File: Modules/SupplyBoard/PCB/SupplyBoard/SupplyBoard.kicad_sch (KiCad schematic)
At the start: 4 parts, among them J1 CI_BATT, J2 USB_B_Mini, U1 STM32L031G6Ux

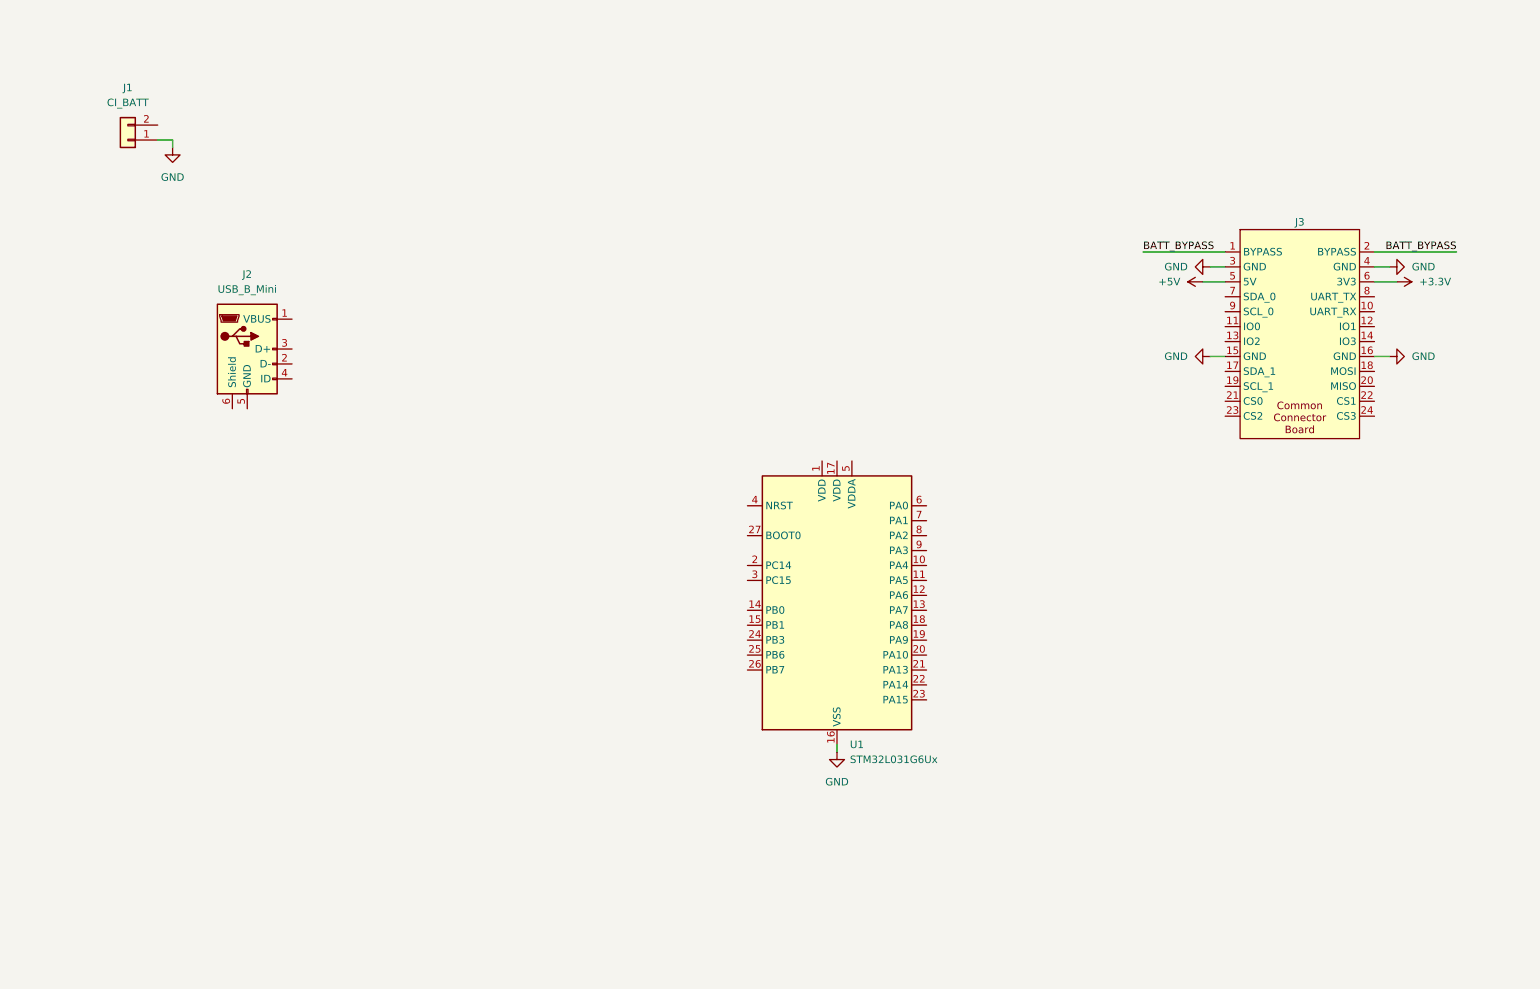
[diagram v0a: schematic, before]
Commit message: [Supply Board] Creados subesquemas
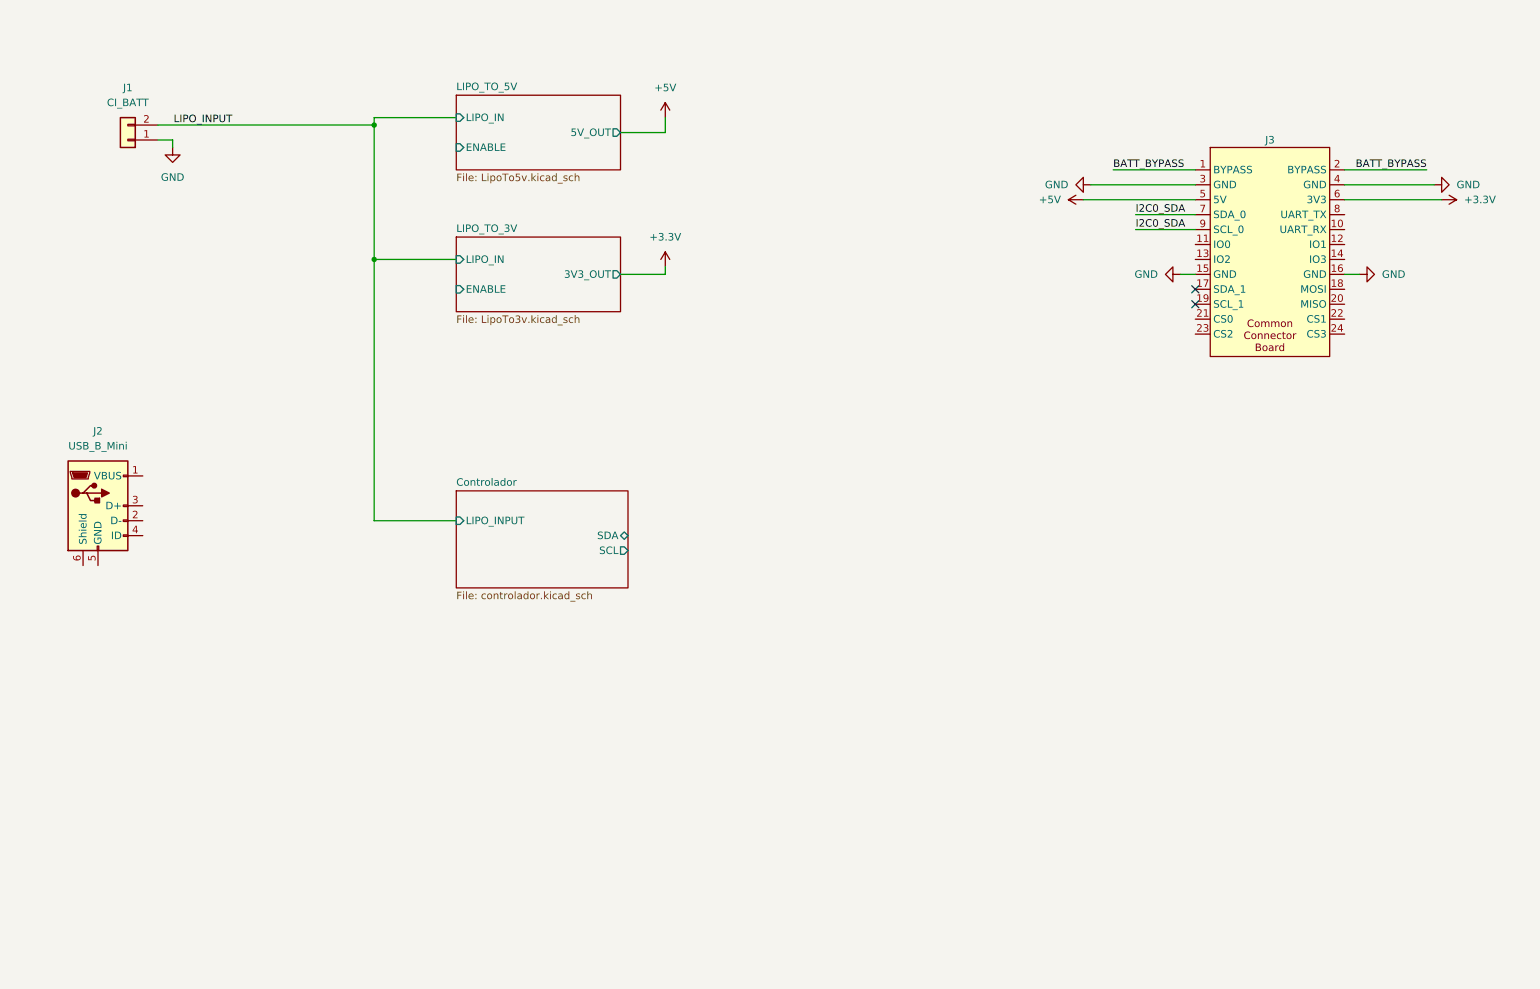
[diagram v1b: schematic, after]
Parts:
- removed U1: STM32L031G6Ux, Package_DFN_QFN:QFN-28_4x4mm_P0.5mm, symbol MCU_ST_STM32L0:STM32L031G6Ux
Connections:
- net LIPO_INPUT: now reaches J1.2 (Pin_2)
- net I2C0_SDA: now reaches J3.7 (SDA_0)
- net I2C0_SDA: now also J3.9 (SCL_0)
- no-connect marks 0 -> 2
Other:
- added sheet Controlador (controlador.kicad_sch)
- added sheet LIPO_TO_3V (LipoTo3v.kicad_sch)
- added sheet LIPO_TO_5V (LipoTo5v.kicad_sch)
- moved on the sheet: J2, J3

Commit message: Lipo to 3v3 circuit added
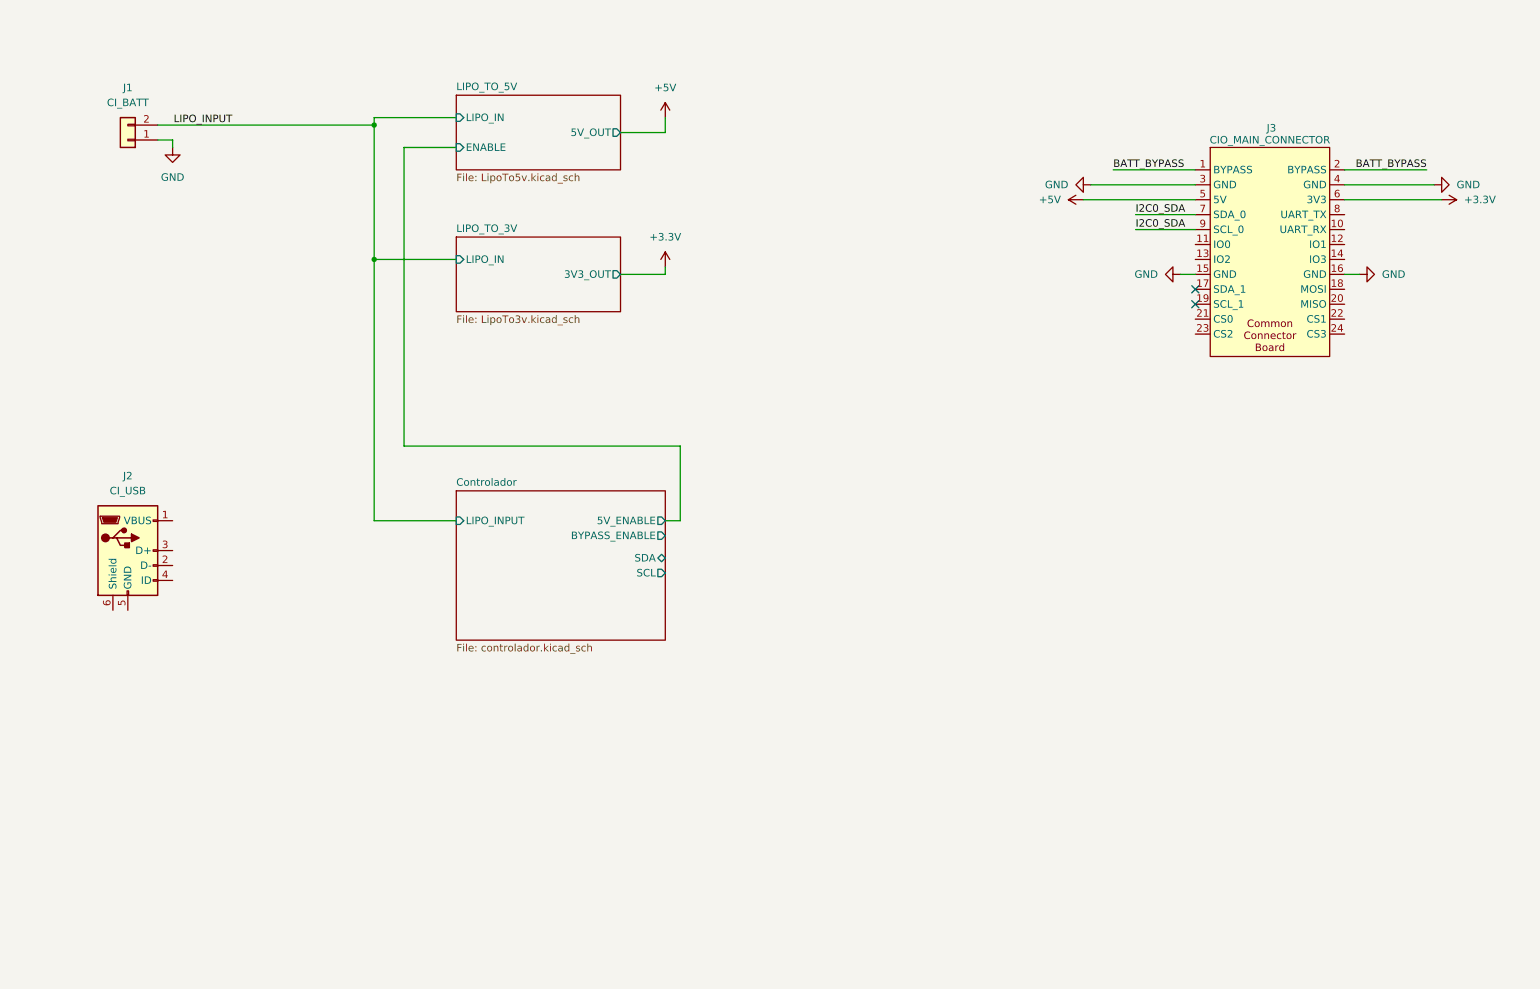
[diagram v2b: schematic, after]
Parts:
- J2: value USB_B_Mini -> CI_USB; footprint Connector_USB:USB_Micro-B_Wuerth_629105150521 -> (none)
- J3: value ~ -> CIO_MAIN_CONNECTOR
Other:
- sheet Controlador ports: added 5V_ENABLE, BYPASS_ENABLE; removed none
- sheet LIPO_TO_3V ports: added none; removed ENABLE
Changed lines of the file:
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@@
+	(wire
+		(pts
+			(xy 137.16 95.25) (xy 90.17 95.25)
+		)
+		(stroke
+			(width 0)
+			(type default)
+		)
+	)
+	(wire
+		(pts
+			(xy 134.62 107.95) (xy 137.16 107.95)
+		)
+		(stroke
+			(width 0)
+			(type default)
+		)
+	)
 	(wire
 		(pts
@@
 	(wire
 		(pts
+			(xy 90.17 44.45) (xy 99.06 44.45)
+		)
+		(stroke
+			(width 0)
+			(type default)
+		)
+	)
+	(wire
+		(pts
 			(xy 250.19 50.8) (xy 265.43 50.8)
 		)
@@
 	(wire
 		(pts
+			(xy 137.16 107.95) (xy 137.16 95.25)
+		)
+		(stroke
+			(width 0)
+			(type default)
+		)
+	)
+	(wire
+		(pts
 			(xy 214.63 55.88) (xy 224.79 55.88)
+		)
+		(stroke
+			(width 0)
+			(type default)
+		)
+	)
+	(wire
+		(pts
+			(xy 90.17 95.25) (xy 90.17 44.45)
 		)
 		(stroke
@@
 	(symbol
 		(lib_id "Connector:USB_B_Mini")
-		(at 38.1 105.41 0)
+		(at 43.18 113.03 0)
 		(unit 1)
 		(exclude_from_sim no)
@@
 		(fields_autoplaced yes)
 		(property "Reference" "J2"
-			(at 38.1 92.71 0)
-			(effects
-				(font
-					(size 1.27 1.27)
-				)
-			)
-		)
-		(property "Value" "USB_B_Mini"
-			(at 38.1 95.25 0)
-			(effects
-				(font
-					(size 1.27 1.27)
-				)
-			)
-		)
-		(property "Footprint" "Connector_USB:USB_Micro-B_Wuerth_629105150521"
-			(at 41.91 106.68 0)
-			(effects
-				(font
-					(size 1.27 1.27)
-				)
-				(hide yes)
-			)
-		)
-		(property "Datasheet" "https://www.lcsc.com/datasheet/lcsc_datasheet_2209301830_SHOU-HAN-MICRO5P-4J-ZB-X_C5184249.pdf"
-			(at 41.91 106.68 0)
+			(at 43.18 100.33 0)
+			(effects
+				(font
+					(size 1.27 1.27)
+				)
+			)
+		)
+		(property "Value" "CI_USB"
+			(at 43.18 102.87 0)
+			(effects
+				(font
+					(size 1.27 1.27)
+				)
+			)
+		)
+		(property "Footprint" ""
+			(at 46.99 114.3 0)
+			(effects
+				(font
+					(size 1.27 1.27)
+				)
+				(hide yes)
+			)
+		)
+		(property "Datasheet" "~"
+			(at 46.99 114.3 0)
 			(effects
 				(font
@@
 		)
 		(property "Description" "USB Mini Type B connector"
-			(at 38.1 105.41 0)
-			(effects
-				(font
-					(size 1.27 1.27)
-				)
-				(hide yes)
-			)
+			(at 43.18 113.03 0)
+			(effects
+				(font
+					(size 1.27 1.27)
+				)
+				(hide yes)
+			)
+		)
+		(pin "4"
 		)
 		(pin "5"
 		)
+		(pin "6"
+		)
 		(pin "2"
 		)
-		(pin "4"
+		(pin "1"
 		)
 		(pin "3"
-		)
-		(pin "6"
-		)
-		(pin "1"
 		)
 		(instances
@@
 		(dnp no)
 		(property "Reference" "J3"
-			(at 237.49 43.18 0)
-			(effects
-				(font
-					(size 1.27 1.27)
-				)
-			)
-		)
-		(property "Value" "~"
+			(at 237.744 41.148 0)
+			(effects
+				(font
+					(size 1.27 1.27)
+				)
+			)
+		)
+		(property "Value" "CIO_MAIN_CONNECTOR"
 			(at 237.49 43.18 0)
 			(effects
@@
 	(sheet
 		(at 99.06 102.87)
-		(size 29.21 16.51)
+		(size 35.56 25.4)
 		(fields_autoplaced yes)
 		(stroke
@@
 		)
 		(property "Sheetfile" "controlador.kicad_sch"
-			(at 99.06 119.9646 0)
+			(at 99.06 128.8546 0)
 			(effects
 				(font
@@
 		)
 		(pin "SCL" output
-			(at 128.27 113.03 0)
+			(at 134.62 116.84 0)
 			(effects
 				(font
@@
 		)
 		(pin "SDA" bidirectional
-			(at 128.27 110.49 0)
+			(at 134.62 114.3 0)
 			(effects
 				(font
@@
 				)
 				(justify left)
+			)
+		)
+		(pin "5V_ENABLE" output
+			(at 134.62 107.95 0)
+			(effects
+				(font
+					(size 1.27 1.27)
+				)
+				(justify right)
+			)
+		)
+		(pin "BYPASS_ENABLE" output
+			(at 134.62 110.49 0)
+			(effects
+				(font
+					(size 1.27 1.27)
+				)
+				(justify right)
 			)
 		)
@@
 			)
 		)
-		(pin "ENABLE" input
-			(at 99.06 68.58 180)
-			(effects
-				(font
-					(size 1.27 1.27)
-				)
-				(justify left)
-			)
-		)

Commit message: SupplyBoard - Added INA2180 current sensor
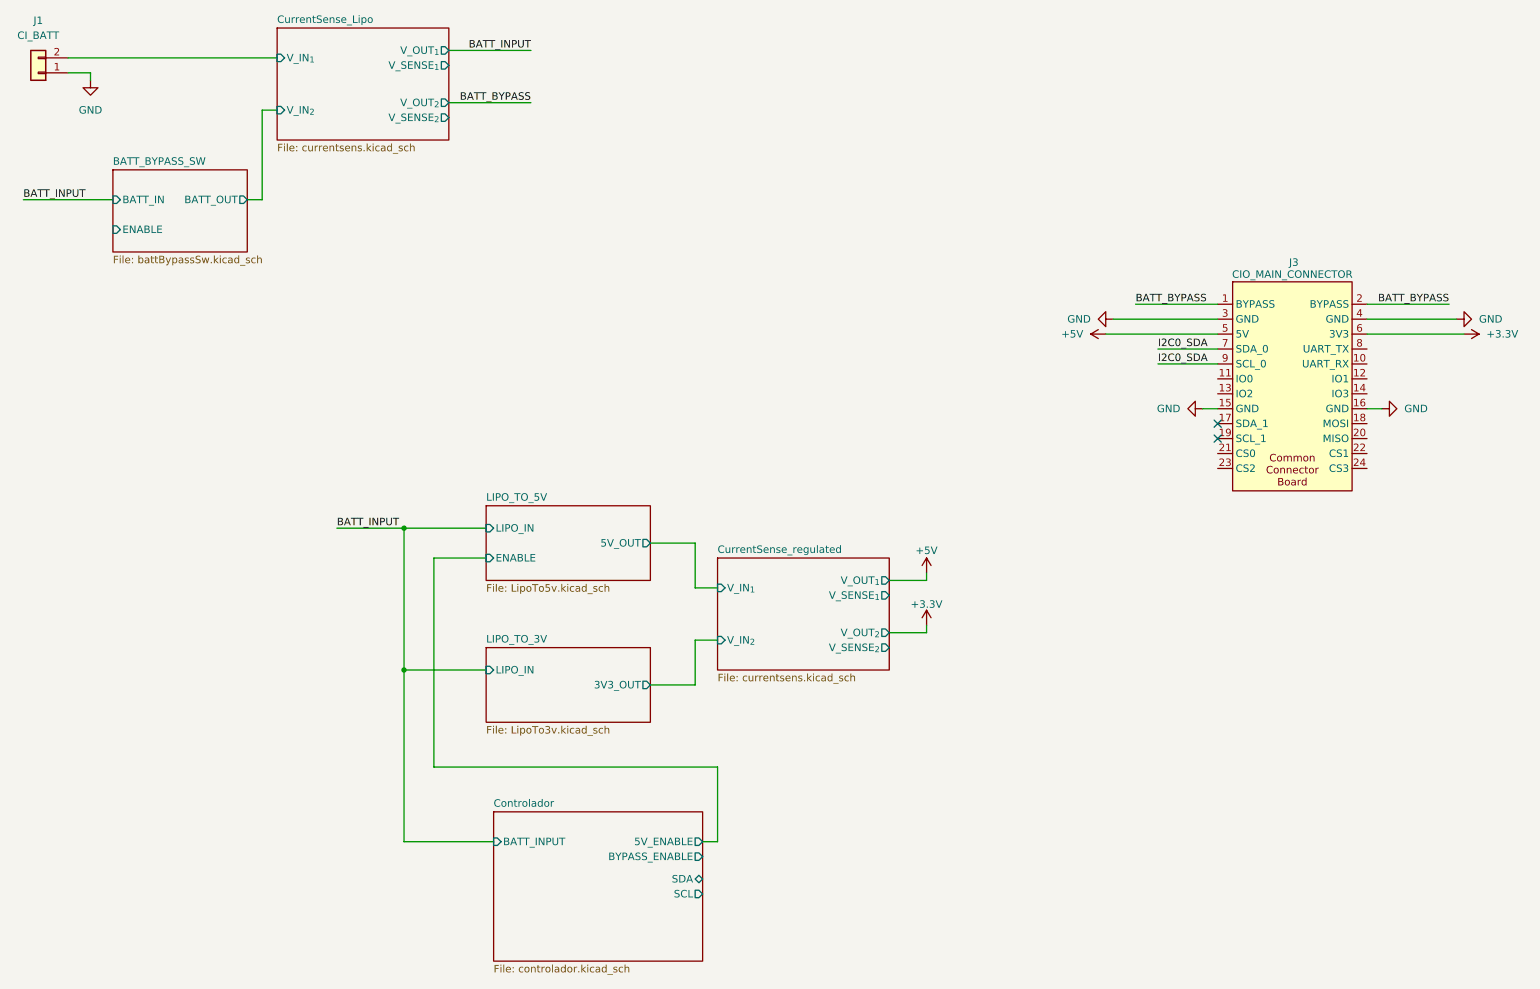
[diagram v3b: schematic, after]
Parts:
- removed J2: CI_USB, symbol Connector:USB_B_Mini
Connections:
- net LIPO_INPUT renamed CurrentSense_Lipo/V_IN_{1}
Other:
- added sheet BATT_BYPASS_SW (battBypassSw.kicad_sch)
- added sheet CurrentSense_Lipo (currentsens.kicad_sch)
- added sheet CurrentSense_regulated (currentsens.kicad_sch)
- sheet Controlador ports: added BATT_INPUT; removed LIPO_INPUT
- moved on the sheet: J1, J3

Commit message: Supply board schematic and PCB
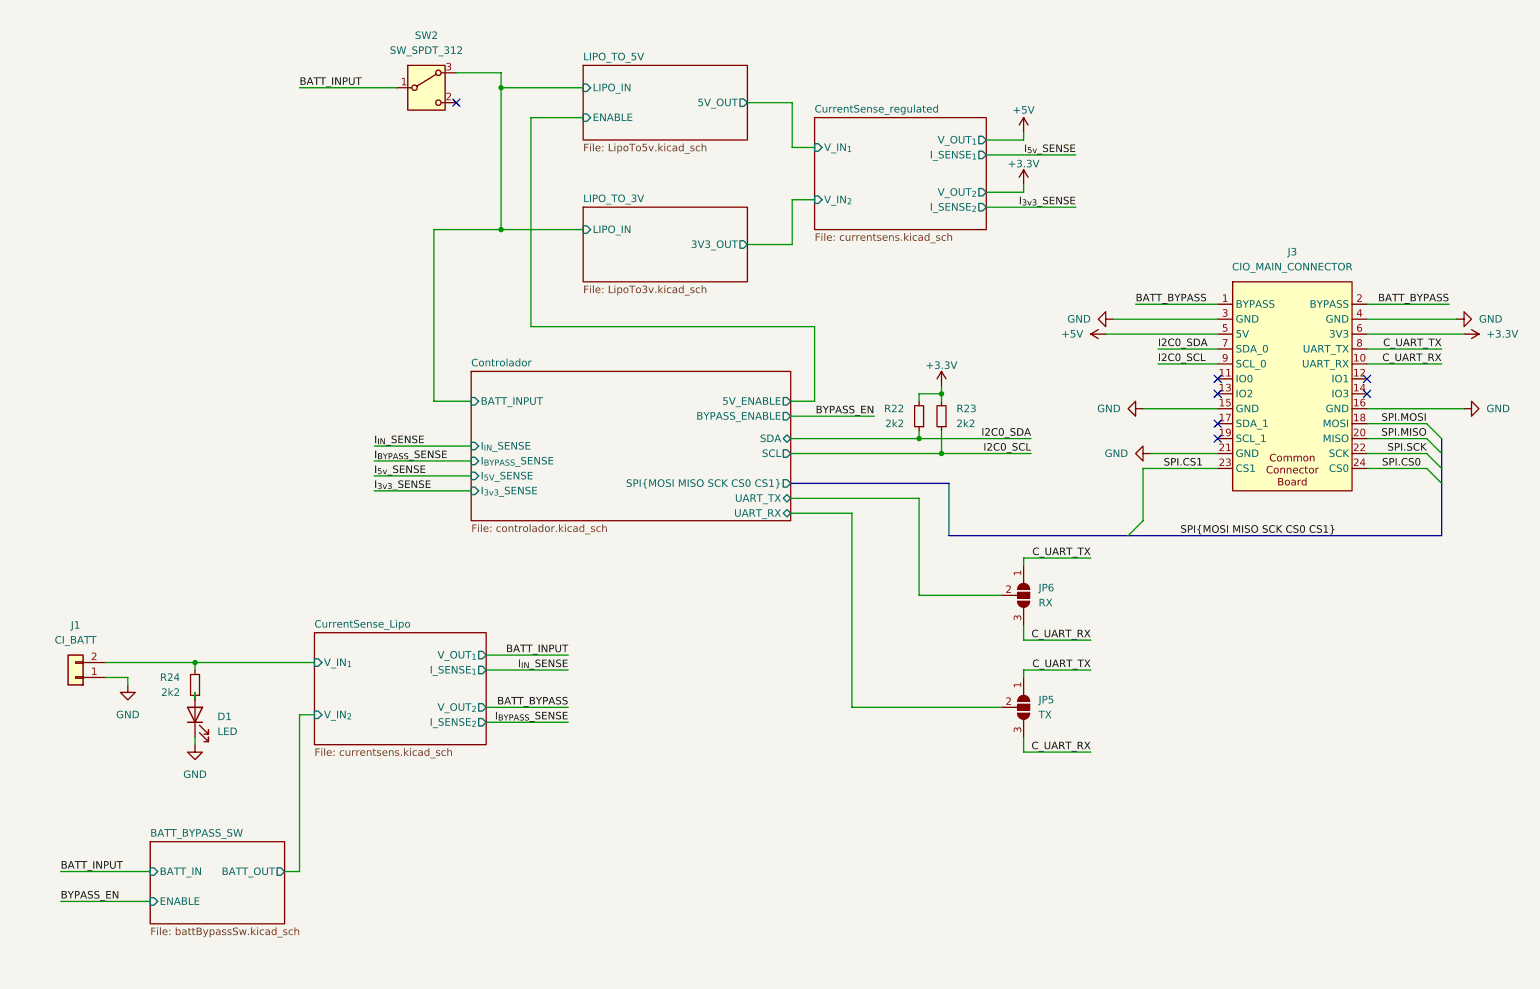
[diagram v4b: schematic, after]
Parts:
- added D1: LED, LED_SMD:LED_0805_2012Metric_Pad1.15x1.40mm_HandSolder, symbol Device:LED
- added JP5: TX, Jumper:SolderJumper-3_P1.3mm_Open_Pad1.0x1.5mm, symbol Jumper:SolderJumper_3_Open
- added JP6: RX, Jumper:SolderJumper-3_P1.3mm_Open_Pad1.0x1.5mm, symbol Jumper:SolderJumper_3_Open
- added R22, R23, R24: 2k2, Resistor_SMD:R_0603_1608Metric_Pad0.98x0.95mm_HandSolder, symbol Device:R_Small
- added SW2: SW_SPDT_312, Connector_PinHeader_2.00mm:PinHeader_1x03_P2.00mm_Vertical, symbol Switch:SW_SPDT_312
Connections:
- net +3.3V: now also R22.2, R23.2
- net BATT_INPUT: now also SW2.1 (B)
- net CurrentSense_Lipo/V_IN_{1}: now also R24.2
- net GND: now also J3.21 (GND), D1.1 (K)
- net I2C0_SDA: now also R22.1; no longer J3.9 (SCL_0)
- net C_UART_RX: now reaches J3.10 (UART_RX)
- net C_UART_RX: now also JP5.3 (B), JP6.3 (B)
- net SPI.MOSI: now reaches J3.18 (MOSI)
- net SPI.MISO: now reaches J3.20 (MISO)
- net SPI.SCK: now reaches J3.22 (SCK)
- net SPI.CS1: now reaches J3.23 (CS1)
- net SPI.CS0: now reaches J3.24 (CS0)
- net C_UART_TX: now reaches J3.8 (UART_TX)
- net C_UART_TX: now also JP5.1 (A), JP6.1 (A)
- new net: D1.2 (A), R24.1
- new net Controlador/BATT_INPUT: SW2.3 (A)
- new net Controlador/UART_RX: JP5.2 (C)
- new net Controlador/UART_TX: JP6.2 (C)
- new net I2C0_SCL: J3.9 (SCL_0), R23.1
- no-connect marks 2 -> 7
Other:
- sheet Controlador ports: added I_{3v3}_SENSE, I_{5V}_SENSE, I_{BYPASS}_SENSE, I_{IN}_SENSE, SPI{MOSI MISO SCK CS0 CS1}, UART_RX, UART_TX; removed none
- sheet CurrentSense_Lipo ports: added I_SENSE_{1}, I_SENSE_{2}; removed V_SENSE_{1}, V_SENSE_{2}
- sheet CurrentSense_regulated ports: added I_SENSE_{1}, I_SENSE_{2}; removed V_SENSE_{1}, V_SENSE_{2}
- moved on the sheet: J1
